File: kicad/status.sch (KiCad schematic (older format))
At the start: 34 parts, among them U28 74HC04, U29 74HC04

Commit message: Update to current kicad libraries
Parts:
- removed D30, D31, D32, D33, D34, D35, D36, D37, D38, D39, D40, D41, D42, D43, D44, D67: LED, LEDs:LED-5MM, symbol LED
- removed R10, R11, R12, R13, R14, R15, R16, R17, R18, R19, R20, R21, R30, R7, R8, R9: 470, Resistors_THT:Resistor_Horizontal_RM7mm, symbol R
- removed U28, U29: 74HC04, Housings_DIP:DIP-14_W7.62mm_LongPads, symbol 74HC04
- added D46, D47, D48, D49, D50, D51, D52, D53, D54, D55, D56, D57, D58, D59, D60, D61: LED, symbol Device:LED
- added R13, R14, R15, R16, R17, R18, R19, R20, R21, R22, R23, R24, R25, R26, R27, R28: 470, symbol Device:R
- added U34, U45, U46, U47, U8: 74LS04, symbol 74xx:74LS04
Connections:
- net labels added: VCC
- wire segments 66 -> 90

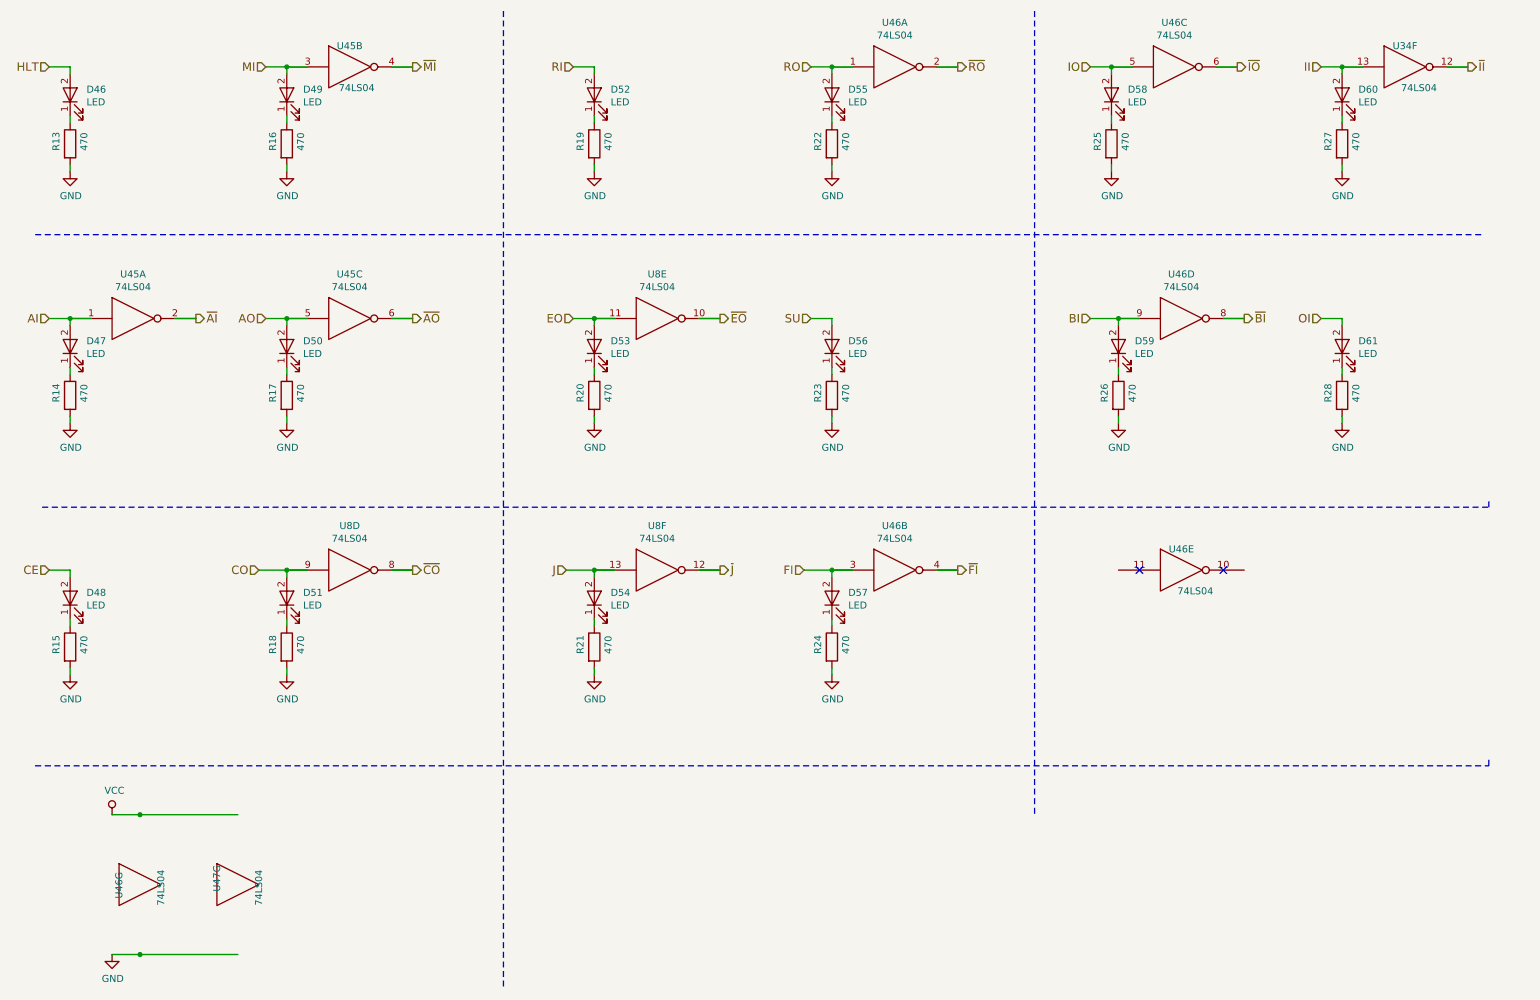
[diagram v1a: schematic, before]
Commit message: update bus names and improve sheet text
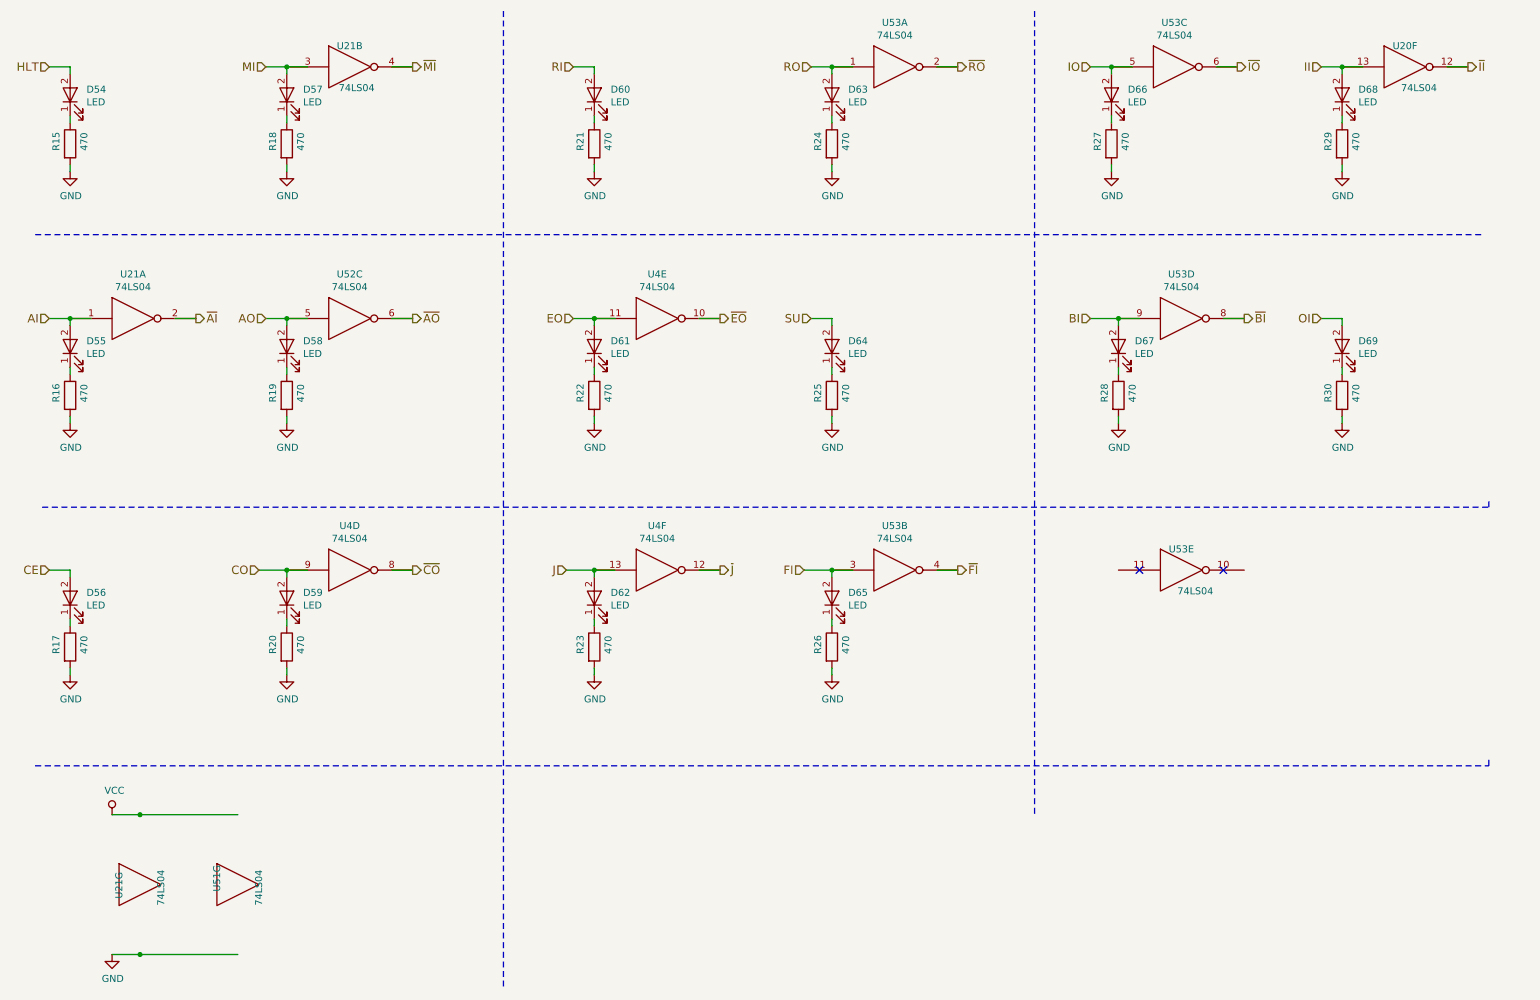
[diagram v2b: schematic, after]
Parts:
- renumbered D46 to D54, D47 to D55, D48 to D56, D49 to D57, D50 to D58, D51 to D59, D52 to D60, D53 to D61, D54 to D62, D55 to D63, D56 to D64, D57 to D65, D58 to D66, D59 to D67, D60 to D68, D61 to D69, R13 to R15, R14 to R16, R15 to R17, R16 to R18, R17 to R19, R18 to R20, R19 to R21, R20 to R22, R21 to R23, R22 to R24, R23 to R25, R24 to R26, R25 to R27, R26 to R28, R27 to R29, R28 to R30, U34 to U20, U45 to U21, U46 to U21, U8 to U4, U47 to U51, U45 to U52, U46 to U53
